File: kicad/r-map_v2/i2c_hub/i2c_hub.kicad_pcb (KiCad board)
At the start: 2 copper layers, 139.7 x 24.1 mm, 110 parts, among them J1 RJ45, J2 RJ45, J3 RJ45, J4 RJ45, J5 RJ45, P1 5V, P10 CONN_01X04, P11 5V, P12 SEL, P13 3V3, P14 CONN_01X04, P15 5V, P16 SEL, P17 3V3, P18 CONN_01X04, P19 5V, P2 SEL, P20 SEL, P21 3V3, P23 CONN_01X04, P24 5V, P25 SEL, P27 3V3, P28 5V, P29 SEL, P3 3V3, P30 3V3, P31 5V, P32 SEL, P33 3V3, P34 5V, P35 SEL, P36 3V3, P37 5V, P38 SEL, P39 3V3, P4 CONN_01X04, P42 5V, P43 SEL, P44 3V3, P45 CONN_01X04, P46 5V, P47 SEL, P48 3V3, P49 CONN_01X04, P50 5V, P51 SEL, P52 3V3, P53 CONN_01X04, P55 5V, P56 SEL, P57 3V3, P59 CONN_01X04, P6 5V, P60 5V, P61 SEL, P62 3V3, P63 CONN_01X04, P7 SEL, P8 3V3, U1 LM317_SOT223, U2 LM317_SOT223, U3 ESDA6V1-5SC6, U4 ESDA6V1-5SC6, U5 ESDA6V1-5SC6, U6 ESDA6V1-5SC6

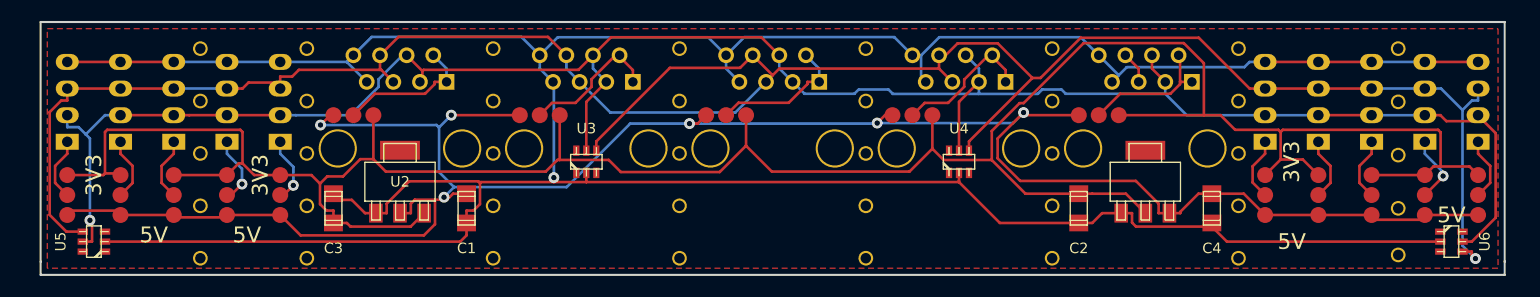
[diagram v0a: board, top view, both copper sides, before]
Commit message: Correzioni su board i2c hub, adattamento per uso cavi RJ11, inserite piste per connessioni GND anche in caso taglio board, ricreazione PCB, inserimento riferimenti autore e licenza.
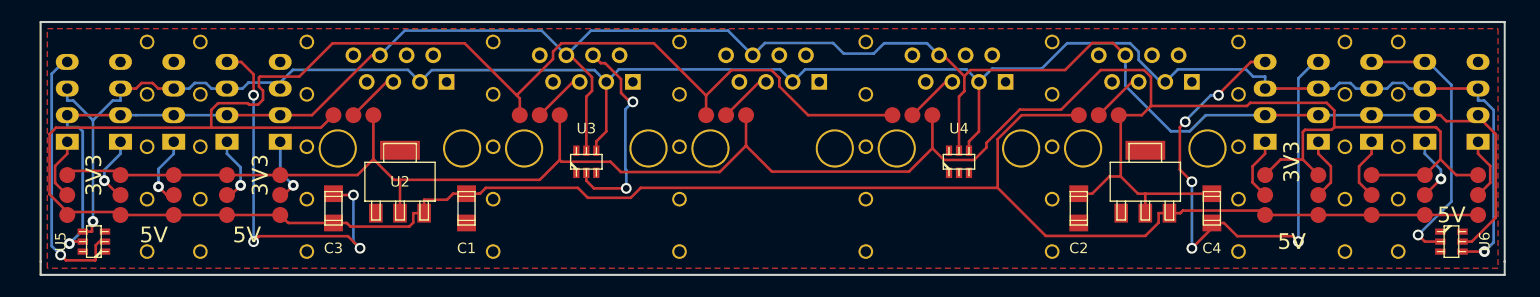
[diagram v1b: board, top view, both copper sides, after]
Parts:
- removed REF**1, REF**10, REF**11, REF**12, REF**13, REF**14, REF**15, REF**16, REF**17, REF**18, REF**19, REF**2, REF**20, REF**21, REF**22, REF**23, REF**24, REF**25, REF**26, REF**27, REF**28, REF**29, REF**3, REF**30, REF**31, REF**32, REF**33, REF**34, REF**35, REF**36, REF**37, REF**38, REF**39, REF**4, REF**40, REF**5, REF**6, REF**7, REF**8, REF**9: 1pin, Connect:1pin
- added REF**1111: 1pin, i2c_hub:1pin, F.Cu at (49.5, 94.6)
- added REF**11111: 1pin, i2c_hub:1pin, F.Cu at (44.5, 94.6)
- added REF**111111: 1pin, i2c_hub:1pin, F.Cu at (59.7, 94.6)
- added REF**111112: 1pin, i2c_hub:1pin, F.Cu at (59.7, 99.6)
- added REF**111113: 1pin, i2c_hub:1pin, F.Cu at (59.7, 104.6)
- added REF**111114: 1pin, i2c_hub:1pin, F.Cu at (59.7, 109.6)
- added REF**111115: 1pin, i2c_hub:1pin, F.Cu at (59.7, 114.6)
- added REF**11112: 1pin, i2c_hub:1pin, F.Cu at (44.5, 99.6)
- added REF**111121: 1pin, i2c_hub:1pin, F.Cu at (77.5, 94.6)
- added REF**111122: 1pin, i2c_hub:1pin, F.Cu at (77.5, 99.6)
- added REF**111123: 1pin, i2c_hub:1pin, F.Cu at (77.5, 104.6)
- added REF**111124: 1pin, i2c_hub:1pin, F.Cu at (77.5, 109.6)
- added REF**111125: 1pin, i2c_hub:1pin, F.Cu at (77.5, 114.6)
- added REF**11113: 1pin, i2c_hub:1pin, F.Cu at (44.5, 104.6)
- added REF**111131: 1pin, i2c_hub:1pin, F.Cu at (95.2, 94.6)
- added REF**111132: 1pin, i2c_hub:1pin, F.Cu at (95.2, 99.6)
- added REF**111133: 1pin, i2c_hub:1pin, F.Cu at (95.2, 104.6)
- added REF**111134: 1pin, i2c_hub:1pin, F.Cu at (95.2, 109.6)
- added REF**111135: 1pin, i2c_hub:1pin, F.Cu at (95.2, 114.6)
- added REF**11114: 1pin, i2c_hub:1pin, F.Cu at (44.5, 109.6)
- added REF**111141: 1pin, i2c_hub:1pin, F.Cu at (113.0, 94.6)
- added REF**111142: 1pin, i2c_hub:1pin, F.Cu at (113.0, 99.6)
- added REF**111143: 1pin, i2c_hub:1pin, F.Cu at (113.0, 104.6)
- added REF**111144: 1pin, i2c_hub:1pin, F.Cu at (113.0, 109.6)
- added REF**111145: 1pin, i2c_hub:1pin, F.Cu at (113.0, 114.6)
- added REF**11115: 1pin, i2c_hub:1pin, F.Cu at (44.5, 114.6)
- added REF**111151: 1pin, i2c_hub:1pin, F.Cu at (130.8, 94.6)
- added REF**111152: 1pin, i2c_hub:1pin, F.Cu at (130.8, 99.6)
- added REF**111153: 1pin, i2c_hub:1pin, F.Cu at (130.8, 104.6)
- added REF**111154: 1pin, i2c_hub:1pin, F.Cu at (130.8, 109.6)
- added REF**111155: 1pin, i2c_hub:1pin, F.Cu at (130.8, 114.6)
- added REF**111161: 1pin, i2c_hub:1pin, F.Cu at (148.6, 94.6)
- added REF**1111611: 1pin, i2c_hub:1pin, F.Cu at (158.8, 94.6)
- added REF**11116111: 1pin, i2c_hub:1pin, F.Cu at (163.8, 94.6)
- added REF**11116112: 1pin, i2c_hub:1pin, F.Cu at (163.8, 99.6)
- added REF**11116113: 1pin, i2c_hub:1pin, F.Cu at (163.8, 104.6)
- added REF**11116114: 1pin, i2c_hub:1pin, F.Cu at (163.8, 109.6)
- added REF**11116115: 1pin, i2c_hub:1pin, F.Cu at (163.8, 114.6)
- added REF**1111612: 1pin, i2c_hub:1pin, F.Cu at (158.8, 99.6)
- added REF**1111613: 1pin, i2c_hub:1pin, F.Cu at (158.8, 104.6)
- added REF**1111614: 1pin, i2c_hub:1pin, F.Cu at (158.8, 109.6)
- added REF**1111615: 1pin, i2c_hub:1pin, F.Cu at (158.8, 114.6)
- added REF**111162: 1pin, i2c_hub:1pin, F.Cu at (148.6, 99.6)
- added REF**111163: 1pin, i2c_hub:1pin, F.Cu at (148.6, 104.6)
- added REF**111164: 1pin, i2c_hub:1pin, F.Cu at (148.6, 109.6)
- added REF**111165: 1pin, i2c_hub:1pin, F.Cu at (148.6, 114.6)
- added REF**1112: 1pin, i2c_hub:1pin, F.Cu at (49.5, 99.6)
- added REF**1113: 1pin, i2c_hub:1pin, F.Cu at (49.5, 104.6)
- added REF**1114: 1pin, i2c_hub:1pin, F.Cu at (49.5, 109.6)
- added REF**1115: 1pin, i2c_hub:1pin, F.Cu at (49.5, 114.6)
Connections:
- C3 pad 1: /+3.3V -> /+5V
- C4 pad 1: /+5V -> /+3.3V
- J1 pad 1: Net-(J1-Pad1) -> (no net)
- J1 pad 2: Net-(J1-Pad1) -> (no net)
- J1 pad 3: /SCL -> /SDA
- J1 pad 4: /SCL -> GND
- J1 pad 5: /SDA -> Net-(J1-Pad5)
- J1 pad 6: /SDA -> /SCL
- J1 pad 7: GND -> (no net)
- J1 pad 8: GND -> (no net)
- J2 pad 1: Net-(J2-Pad1) -> (no net)
- J2 pad 2: Net-(J2-Pad1) -> (no net)
- J2 pad 3: /SCL -> /SDA
- J2 pad 4: /SCL -> GND
- J2 pad 5: /SDA -> Net-(J2-Pad5)
- J2 pad 6: /SDA -> /SCL
- J2 pad 7: GND -> (no net)
- J2 pad 8: GND -> (no net)
- J3 pad 1: Net-(J3-Pad1) -> (no net)
- J3 pad 2: Net-(J3-Pad1) -> (no net)
- J3 pad 3: /SCL -> /SDA
- J3 pad 4: /SCL -> GND
- J3 pad 5: /SDA -> Net-(J3-Pad5)
- J3 pad 6: /SDA -> /SCL
- J3 pad 7: GND -> (no net)
- J3 pad 8: GND -> (no net)
- J4 pad 1: Net-(J4-Pad1) -> (no net)
- J4 pad 2: Net-(J4-Pad1) -> (no net)
- J4 pad 3: /SCL -> /SDA
- J4 pad 4: /SCL -> GND
- J4 pad 5: /SDA -> Net-(J4-Pad5)
- J4 pad 6: /SDA -> /SCL
- J4 pad 7: GND -> (no net)
- J4 pad 8: GND -> (no net)
- J5 pad 1: Net-(J5-Pad1) -> (no net)
- J5 pad 2: Net-(J5-Pad1) -> (no net)
- J5 pad 3: /SCL -> /SDA
- J5 pad 4: /SCL -> GND
- J5 pad 6: Net-(J5-Pad5) -> /SCL
- J5 pad 7: GND -> (no net)
- J5 pad 8: GND -> (no net)
- P25 pad 1: Net-(J1-Pad1) -> Net-(J1-Pad5)
- P29 pad 1: Net-(J2-Pad1) -> Net-(J2-Pad5)
- P32 pad 1: Net-(J3-Pad1) -> Net-(J3-Pad5)
- P35 pad 1: Net-(J4-Pad1) -> Net-(J4-Pad5)
- P38 pad 1: Net-(J5-Pad1) -> Net-(J5-Pad5)
- U2 pad 2: /+5V -> /+3.3V
- U2 pad 3: /+3.3V -> /+5V
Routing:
- net GND: track 319.0 -> 161.9 mm, vias 1 -> 13
- net /+5V: track 198.1 -> 277.0 mm, vias 6 -> 0
- net /+3.3V: track 242.7 -> 215.7 mm
- net /SDA: track 221.1 -> 194.8 mm, vias 1 -> 2
- net Net-(J2-Pad1): track 13.5 -> 0.00 mm
- net Net-(J4-Pad1): track 13.4 -> 0.00 mm
- net Net-(J1-Pad1): track 13.4 -> 0.00 mm
- net Net-(J3-Pad1): track 13.4 -> 0.00 mm
- net Net-(J5-Pad1): track 12.9 -> 0.00 mm
- net Net-(J4-Pad5): track 0.00 -> 5.13 mm
- net Net-(J3-Pad5): track 0.00 -> 5.13 mm
- net Net-(J2-Pad5): track 0.00 -> 5.13 mm
- net Net-(J1-Pad5): track 0.00 -> 5.13 mm
- net Net-(J5-Pad5): track 3.07 -> 5.13 mm
- net /SCL: track 199.9 -> 199.0 mm
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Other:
- board text added: "VCC"
- board text removed: "VIN"

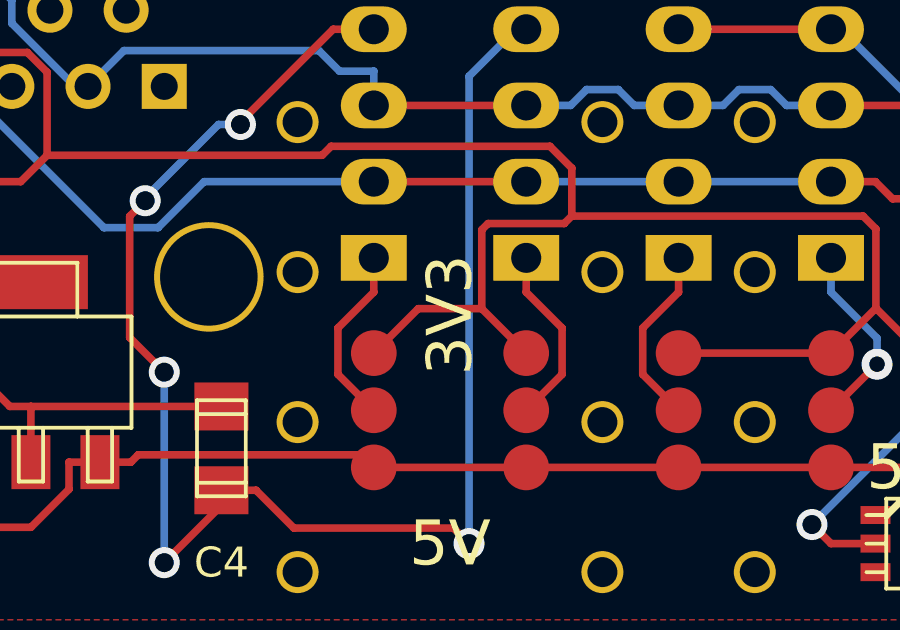
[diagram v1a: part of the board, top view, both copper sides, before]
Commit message: Modifiche a schema elettrico su modulo bluethoot, modificate connessioni per seriale 1. Modulo stima-i2c modificati pin per rele' e aggiunte connessioni esd su alimentazione. Rigenerati pcb.
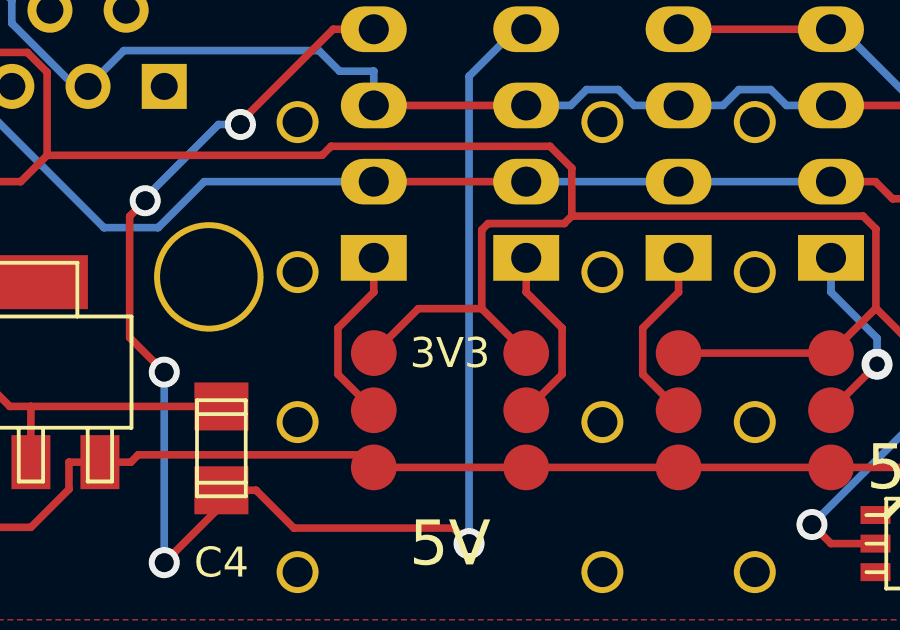
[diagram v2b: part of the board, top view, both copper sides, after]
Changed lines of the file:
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@@
     (pad 1 thru_hole circle (at 0 0) (size 1.4 1.4) (drill 1) (layers *.Cu *.Mask F.SilkS))
   )
-  (gr_text 3V3 (at 153.67 106.045 90) (layer F.SilkS)
-    (effects (font (size 1.5 1.5) (thickness 0.3)))
+  (gr_text 3V3 (at 153.67 107.315) (layer F.SilkS)
+    (effects (font (size 1 1) (thickness 0.16)))
   )
   (gr_text 5V (at 168.91 111.125) (layer F.SilkS)
@@
     (effects (font (size 1.5 1.5) (thickness 0.3)) (justify mirror))
   )
-  (gr_text VCC (at 158.75 106.68 90) (layer B.SilkS)
-    (effects (font (size 1.5 1.5) (thickness 0.3)) (justify mirror))
+  (gr_text VCC (at 153.67 109.22) (layer B.SilkS)
+    (effects (font (size 1 1) (thickness 0.16)) (justify mirror))
   )
   (gr_line (start 34.29 115.57) (end 34.29 116.84) (angle 90) (layer Edge.Cuts) (width 0.2))

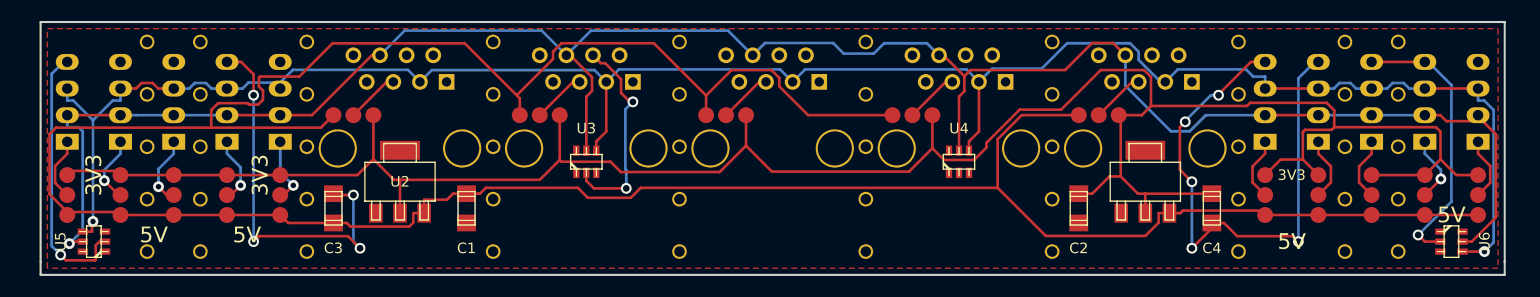
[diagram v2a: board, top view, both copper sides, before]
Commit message: Aggiunto ponticello a saldare per uscita 3.3V. Nuovo design per i2chub
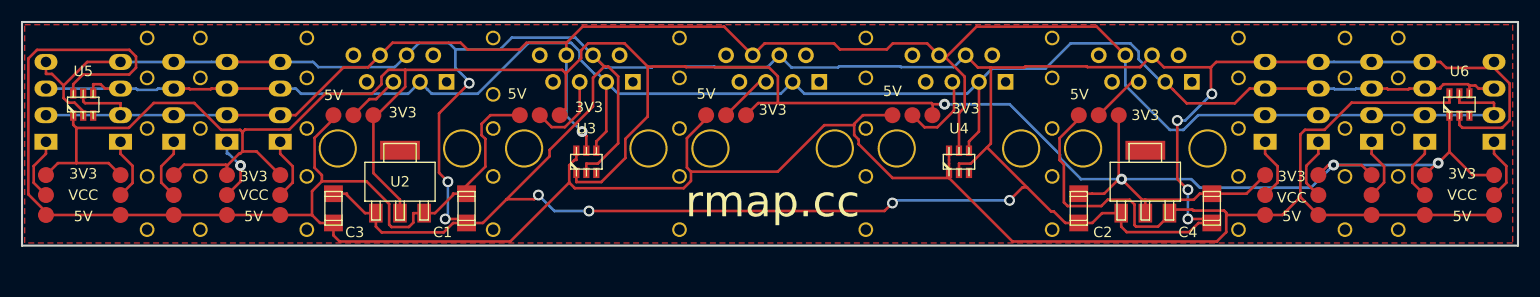
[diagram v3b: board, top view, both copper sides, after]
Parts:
- moved U5 13.1 mm to (38.4, 100.6), turned to 0 degrees
- moved U6 13.1 mm to (169.7, 100.6), turned to 0 degrees
- moved REF**111135 2.35 mm to (95.2, 112.3)
- moved REF**111145 2.35 mm to (113.0, 112.3)
- moved REF**111155 2.35 mm to (130.8, 112.3)
- moved REF**111165 2.35 mm to (148.6, 112.3)
- moved REF**111164 2.17 mm to (148.6, 107.4)
- moved REF**111115 2.09 mm to (59.7, 112.5)
- moved REF**111125 2.09 mm to (77.5, 112.5)
- moved REF**11115 2.09 mm to (44.5, 112.5)
- moved REF**11116115 2.09 mm to (163.8, 112.5)
- moved REF**1111615 2.09 mm to (158.8, 112.5)
- moved REF**1115 2.09 mm to (49.5, 112.5)
- moved P60 2.03 mm to (34.8, 111.1)
- moved P61 2.03 mm to (34.8, 109.2)
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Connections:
- J1 pad 1: (no net) -> Net-(J1-Pad1)
- J1 pad 2: (no net) -> Net-(J1-Pad2)
- J1 pad 7: (no net) -> Net-(J1-Pad7)
- J1 pad 8: (no net) -> Net-(J1-Pad8)
- J2 pad 1: (no net) -> Net-(J2-Pad1)
- J2 pad 2: (no net) -> Net-(J2-Pad2)
- J2 pad 7: (no net) -> Net-(J2-Pad7)
- J2 pad 8: (no net) -> Net-(J2-Pad8)
- J3 pad 1: (no net) -> Net-(J3-Pad1)
- J3 pad 2: (no net) -> Net-(J3-Pad2)
- J3 pad 7: (no net) -> Net-(J3-Pad7)
- J3 pad 8: (no net) -> Net-(J3-Pad8)
- J4 pad 1: (no net) -> Net-(J4-Pad1)
- J4 pad 2: (no net) -> Net-(J4-Pad2)
- J4 pad 7: (no net) -> Net-(J4-Pad7)
- J4 pad 8: (no net) -> Net-(J4-Pad8)
- J5 pad 1: (no net) -> Net-(J5-Pad1)
- J5 pad 2: (no net) -> Net-(J5-Pad2)
- J5 pad 7: (no net) -> Net-(J5-Pad7)
- J5 pad 8: (no net) -> Net-(J5-Pad8)
- U3 pad 1: (no net) -> /+3.3V
- U3 pad 3: (no net) -> Net-(U3-Pad3)
- U3 pad 6: (no net) -> /+5V
- U4 pad 1: (no net) -> /+5V
- U4 pad 3: (no net) -> Net-(U4-Pad3)
- U4 pad 6: (no net) -> /+5V
- U5 pad 1: (no net) -> /+3.3V
- U5 pad 3: (no net) -> Net-(U5-Pad3)
- U5 pad 6: (no net) -> /+5V
- U6 pad 1: (no net) -> /+3.3V
- U6 pad 3: (no net) -> Net-(U6-Pad3)
- U6 pad 6: (no net) -> /+5V
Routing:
- net GND: track 161.9 -> 344.4 mm, vias 13 -> 11
- net /+3.3V: track 215.7 -> 259.1 mm, vias 0 -> 4
- net /SDA: track 194.8 -> 169.1 mm, vias 2 -> 0
- net /+5V: track 277.0 -> 298.4 mm
- net /SCL: track 199.0 -> 184.2 mm
- net Net-(J4-Pad5): track 5.13 -> 7.91 mm
- net Net-(J2-Pad5): track 5.13 -> 7.77 mm
- net Net-(P51-Pad1): track 6.67 -> 6.07 mm, vias 1 -> 0
- net Net-(P56-Pad1): track 6.45 -> 6.03 mm, vias 1 -> 0
- net Net-(P16-Pad1): track 6.35 -> 6.07 mm, vias 1 -> 0
- net Net-(P43-Pad1): track 6.31 -> 6.07 mm, vias 1 -> 0
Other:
- board size 139.7 x 24.1 mm -> 142.7 x 21.3 mm
- board text added: "rmap.cc"

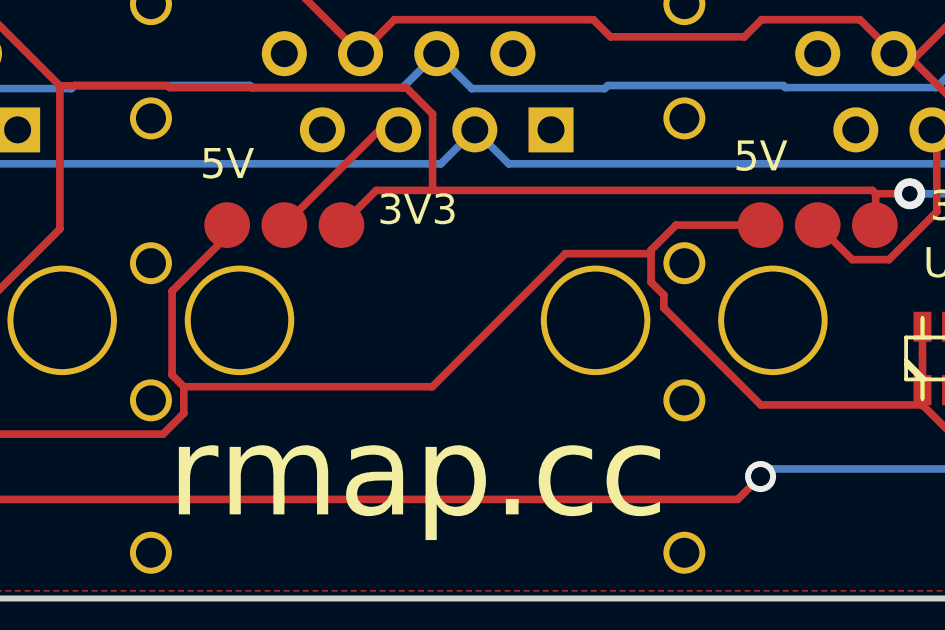
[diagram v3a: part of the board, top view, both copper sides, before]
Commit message: Spostata una pista per evitare interruzioni in caso di sezionamento borad
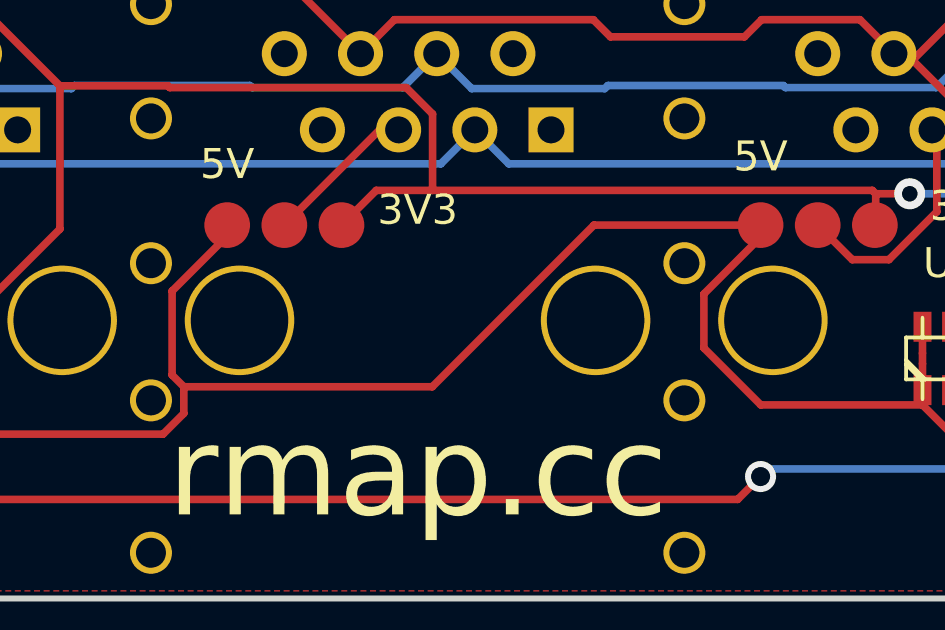
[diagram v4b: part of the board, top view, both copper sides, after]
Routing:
- net /+5V: track 298.4 -> 299.3 mm
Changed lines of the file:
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@@
-(kicad_pcb (version 4) (host pcbnew 0.201509030901+6151~29~ubuntu14.04.1-product)
+(kicad_pcb (version 4) (host pcbnew 0.201601131446+6458~42~ubuntu14.04.1-product)
   (general
     (links 119)
     (no_connects 0)
-    (area 32.411999 92.609999 175.360001 114.146001)
+    (area 32.411999 87.122 177.5968 116.345)
     (thickness 1.6)
     (drawings 39)
-    (tracks 556)
+    (tracks 553)
     (zones 0)
     (modules 120)
@@
     (visible_elements 7FFEF67D)
     (pcbplotparams
-      (layerselection 0x010f0_80000001)
+      (layerselection 0x010f0_ffffffff)
       (usegerberextensions false)
       (excludeedgelayer true)
@@
   (segment (start 138.43 98.425) (end 139.065 98.425) (width 0.254) (layer F.Cu) (net 12))
   (segment (start 135.255 101.6) (end 138.43 98.425) (width 0.254) (layer F.Cu) (net 12))
+  (segment (start 120.9675 107.5933) (end 115.5768 107.5933) (width 0.254) (layer F.Cu) (net 13))
+  (segment (start 115.5768 107.5933) (end 113.680898 105.697398) (width 0.254) (layer F.Cu) (net 13))
+  (segment (start 113.680898 105.697398) (end 113.680898 103.895502) (width 0.254) (layer F.Cu) (net 13))
+  (segment (start 113.680898 103.895502) (end 115.57 102.0064) (width 0.254) (layer F.Cu) (net 13))
+  (segment (start 115.57 102.0064) (end 115.57 101.6) (width 0.254) (layer F.Cu) (net 13))
+  (segment (start 115.57 101.6) (end 110.0162 101.6) (width 0.254) (layer F.Cu) (net 13))
+  (segment (start 110.0162 101.6) (end 104.6282 106.988) (width 0.254) (layer F.Cu) (net 13))
+  (segment (start 104.6282 106.988) (end 96.3447 106.988) (width 0.254) (layer F.Cu) (net 13))
   (segment (start 147.4209 110.9152) (end 147.4209 111.125) (width 0.254) (layer F.Cu) (net 13))
   (segment (start 147.2112 110.7055) (end 147.4209 110.9152) (width 0.254) (layer F.Cu) (net 13))
@@
   (segment (start 96.3447 106.988) (end 96.3447 107.8764) (width 0.254) (layer F.Cu) (net 13))
   (segment (start 120.9675 107.1016) (end 120.9675 107.5933) (width 0.254) (layer F.Cu) (net 13))
-  (segment (start 109.0645 102.5517) (end 111.9197 102.5517) (width 0.254) (layer F.Cu) (net 13))
-  (segment (start 104.6282 106.988) (end 109.0645 102.5517) (width 0.254) (layer F.Cu) (net 13))
-  (segment (start 96.3447 106.988) (end 104.6282 106.988) (width 0.254) (layer F.Cu) (net 13))
-  (segment (start 111.9197 103.5035) (end 111.9197 102.5517) (width 0.254) (layer F.Cu) (net 13))
-  (segment (start 112.3468 103.9306) (end 111.9197 103.5035) (width 0.254) (layer F.Cu) (net 13))
-  (segment (start 112.3468 104.3633) (end 112.3468 103.9306) (width 0.254) (layer F.Cu) (net 13))
-  (segment (start 115.5768 107.5933) (end 112.3468 104.3633) (width 0.254) (layer F.Cu) (net 13))
-  (segment (start 120.9675 107.5933) (end 115.5768 107.5933) (width 0.254) (layer F.Cu) (net 13))
-  (segment (start 112.7523 101.6) (end 115.57 101.6) (width 0.254) (layer F.Cu) (net 13))
-  (segment (start 111.9197 102.4326) (end 112.7523 101.6) (width 0.254) (layer F.Cu) (net 13))
-  (segment (start 111.9197 102.5517) (end 111.9197 102.4326) (width 0.254) (layer F.Cu) (net 13))
   (segment (start 147.4209 111.125) (end 151.13 111.125) (width 0.254) (layer F.Cu) (net 13))
   (segment (start 127.0288 113.6546) (end 120.9675 107.5933) (width 0.254) (layer F.Cu) (net 13))
